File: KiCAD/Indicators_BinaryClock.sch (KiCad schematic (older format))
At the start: 54 parts, among them Q1 ZTX457, Q10 ZTX457, Q11 ZTX457, Q12 ZTX457, Q13 ZTX457, Q2 2N3904, Q3 2N3904, Q4 2N3904, Q5 2N3904, Q6 ZTX457, Q7 ZTX457, Q8 ZTX457, Q9 ZTX457

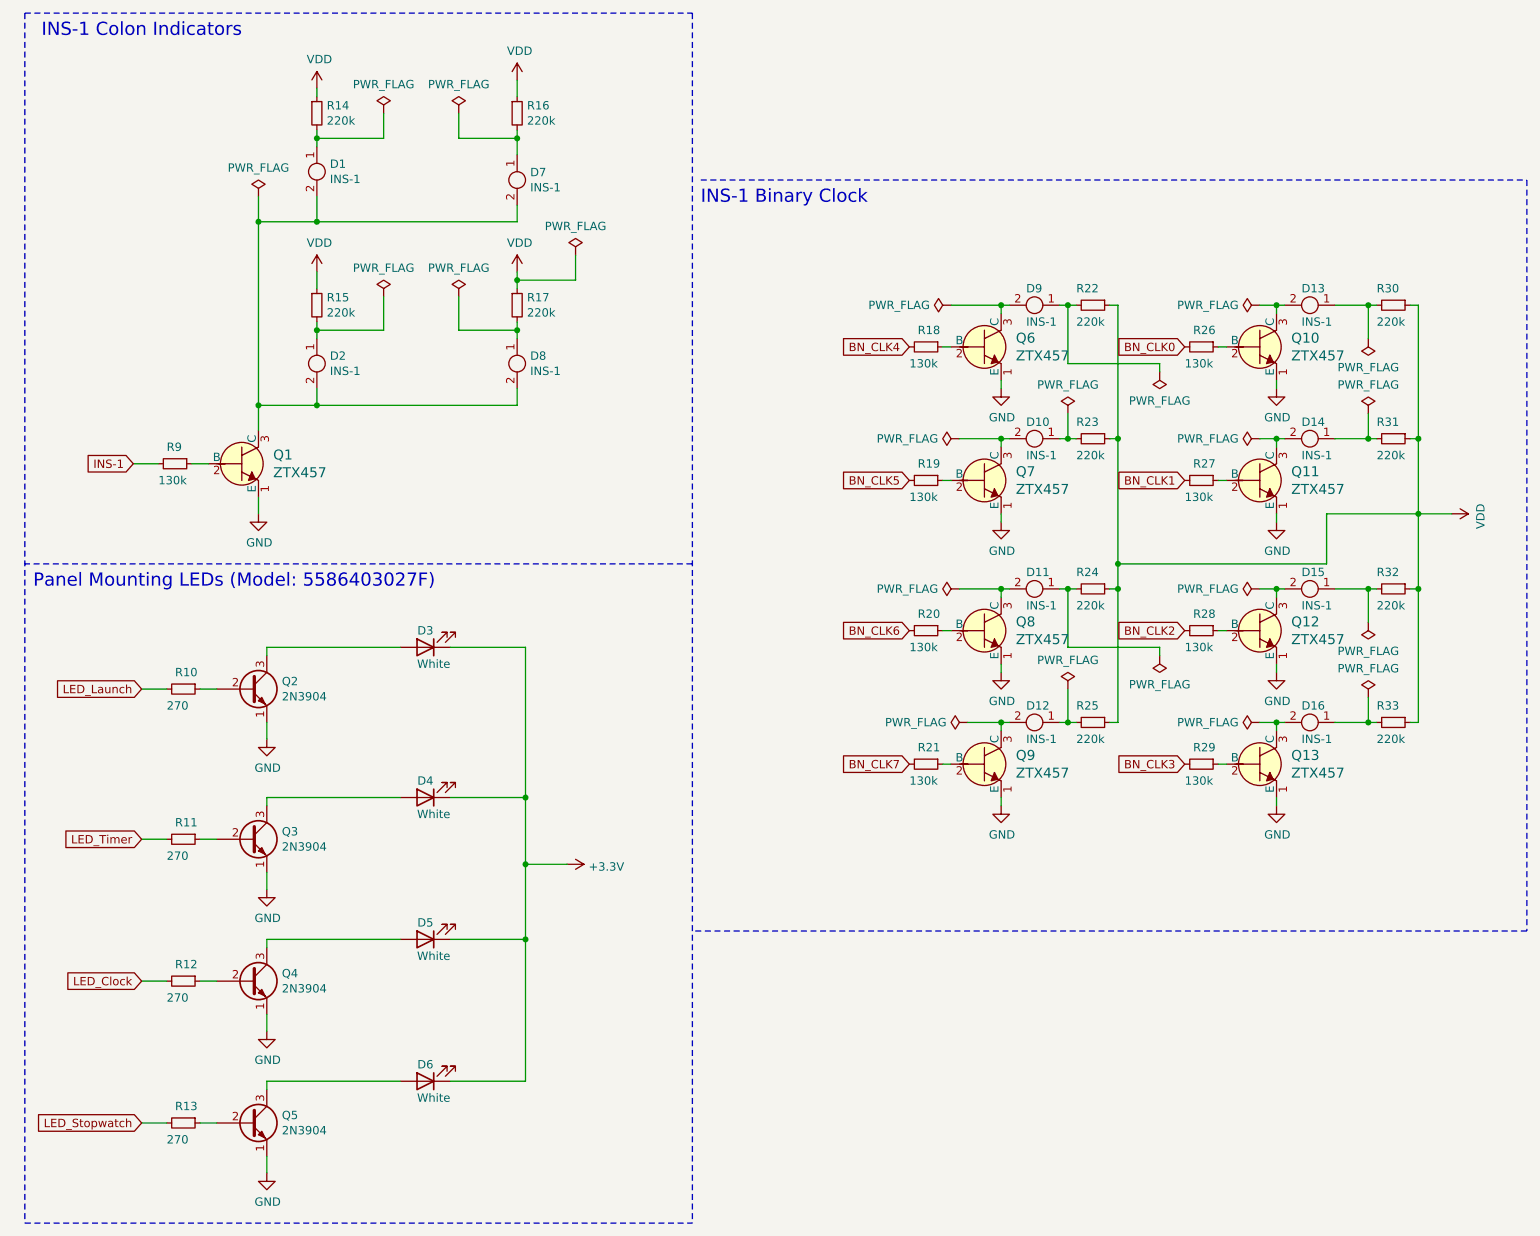
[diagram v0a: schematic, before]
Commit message: v01.2: Updated component numbers, title block, and added transistor library.
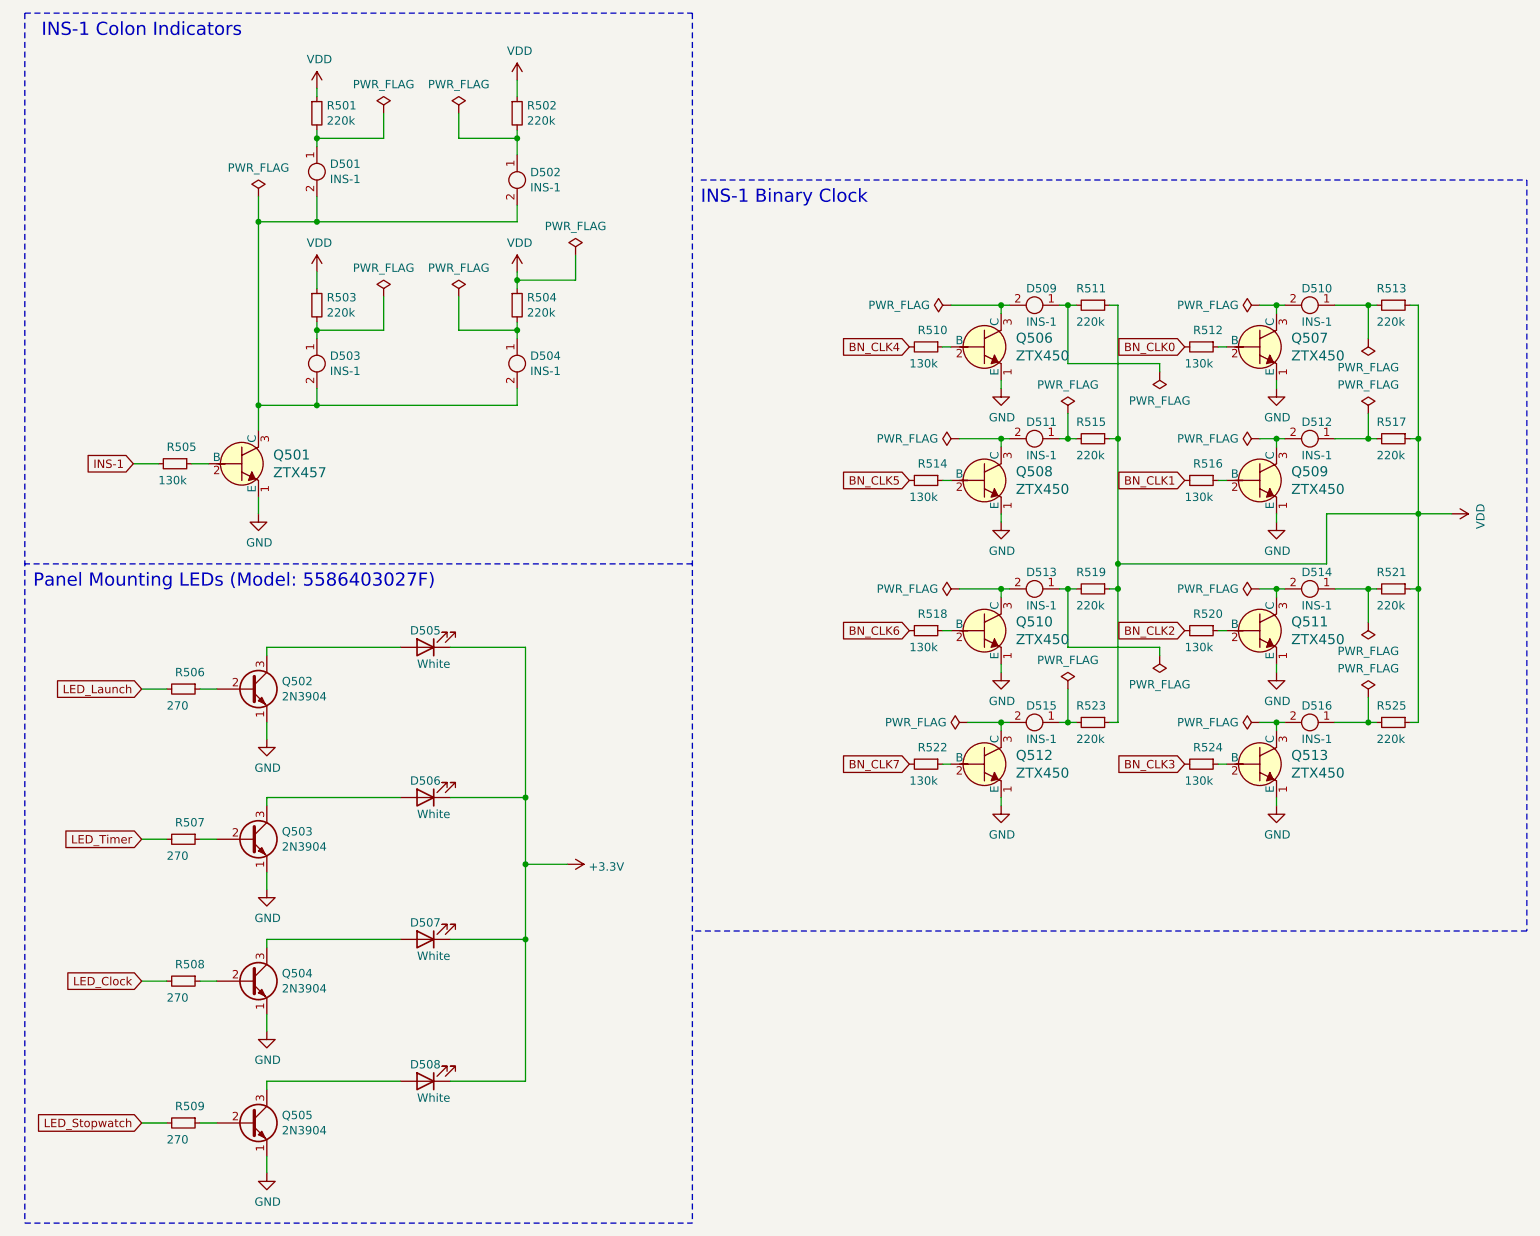
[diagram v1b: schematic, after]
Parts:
- removed Q10, Q11, Q12, Q13, Q6, Q7, Q8, Q9: ZTX457, digikey-footprints:TO-92-3, symbol dk_Transistors-Bipolar-BJT-Single:ZTX450
- added Q506, Q507, Q508, Q509, Q510, Q511, Q512, Q513: ZTX450, digikey-footprints:TO-92-3, symbol dk_Transistors-Bipolar-BJT-Single:ZTX450
- renumbered D1 to D501, D7 to D502, D2 to D503, D8 to D504, D3 to D505, D4 to D506, D5 to D507, D6 to D508, D9 to D509, D13 to D510, D10 to D511, D14 to D512, D11 to D513, D15 to D514, D12 to D515, D16 to D516, Q1 to Q501, Q2 to Q502, Q3 to Q503, Q4 to Q504, Q5 to Q505, R14 to R501, R16 to R502, R15 to R503, R17 to R504, R9 to R505, R10 to R506, R11 to R507, R12 to R508, R13 to R509, R18 to R510, R22 to R511, R26 to R512, R30 to R513, R19 to R514, R23 to R515, R27 to R516, R31 to R517, R20 to R518, R24 to R519, R28 to R520, R32 to R521, R21 to R522, R25 to R523, R29 to R524, R33 to R525
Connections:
- net GND: now also Q506.1 (E), Q507.1 (E), Q508.1 (E), Q509.1 (E), Q510.1 (E), Q511.1 (E), Q512.1 (E), Q513.1 (E)
- net at D510.2: now also Q507.3 (C)
- net at D509.2: now also Q506.3 (C)
- net at D515.2: now also Q512.3 (C)
- net at D513.2: now also Q510.3 (C)
- net at D512.2: now also Q509.3 (C)
- net at D511.2: now also Q508.3 (C)
- net at R512.1: now also Q507.2 (B)
- net at D514.2: now also Q511.3 (C)
- net at R516.1: now also Q509.2 (B)
- net at R520.1: now also Q511.2 (B)
- net at D516.2: now also Q513.3 (C)
- net at R524.1: now also Q513.2 (B)
- net at R522.1: now also Q512.2 (B)
- net at R518.1: now also Q510.2 (B)
- net at R514.1: now also Q508.2 (B)
- net at R510.1: now also Q506.2 (B)
